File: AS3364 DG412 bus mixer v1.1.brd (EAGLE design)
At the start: 81.3 x 36.8 mm, 123 parts, among them IC1 PCA9539PW, IC10 DG412-J, IC11 DG412-J, IC2 TL074JT, IC3 TL072JT, IC4 TL074JT, IC5 TL072JT, IC6 TL072JT, IC8 DG412-J, IC9 DG412-J

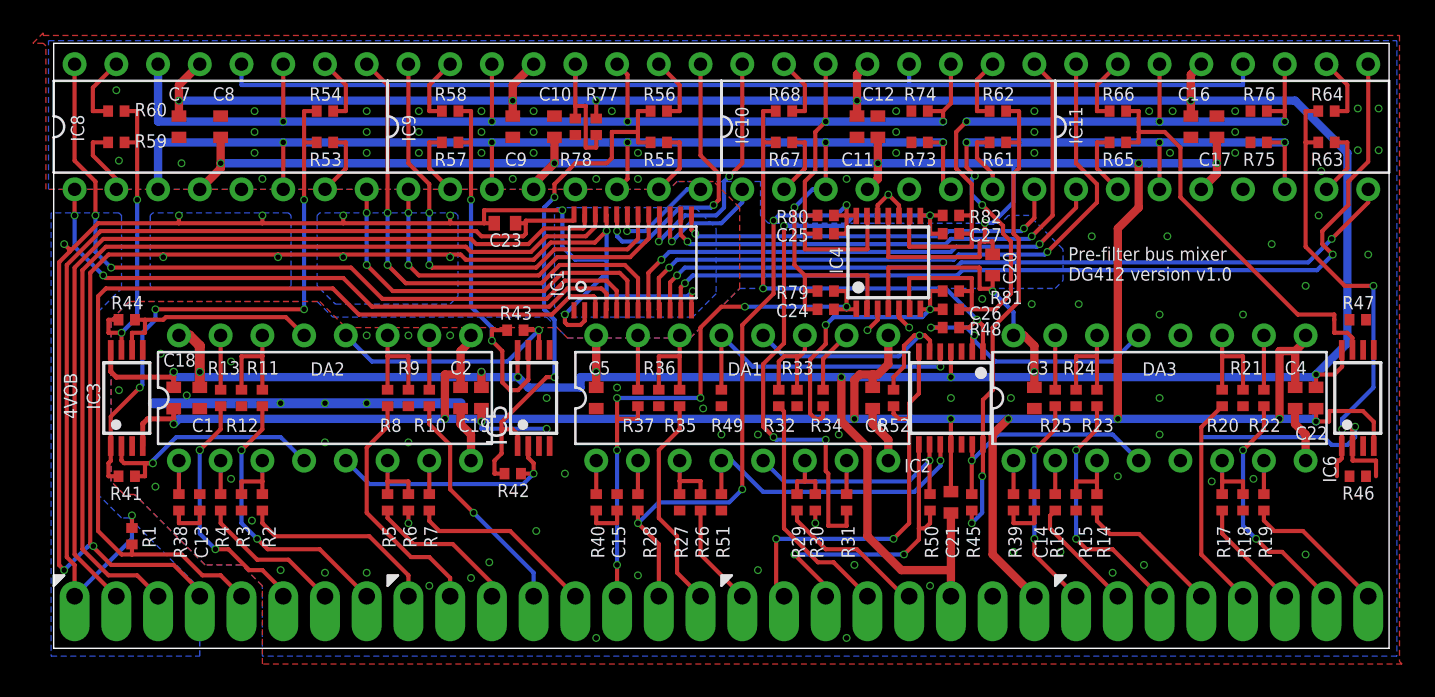
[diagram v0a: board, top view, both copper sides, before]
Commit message: Finished tracing v1.1 of DG412 bus mixer
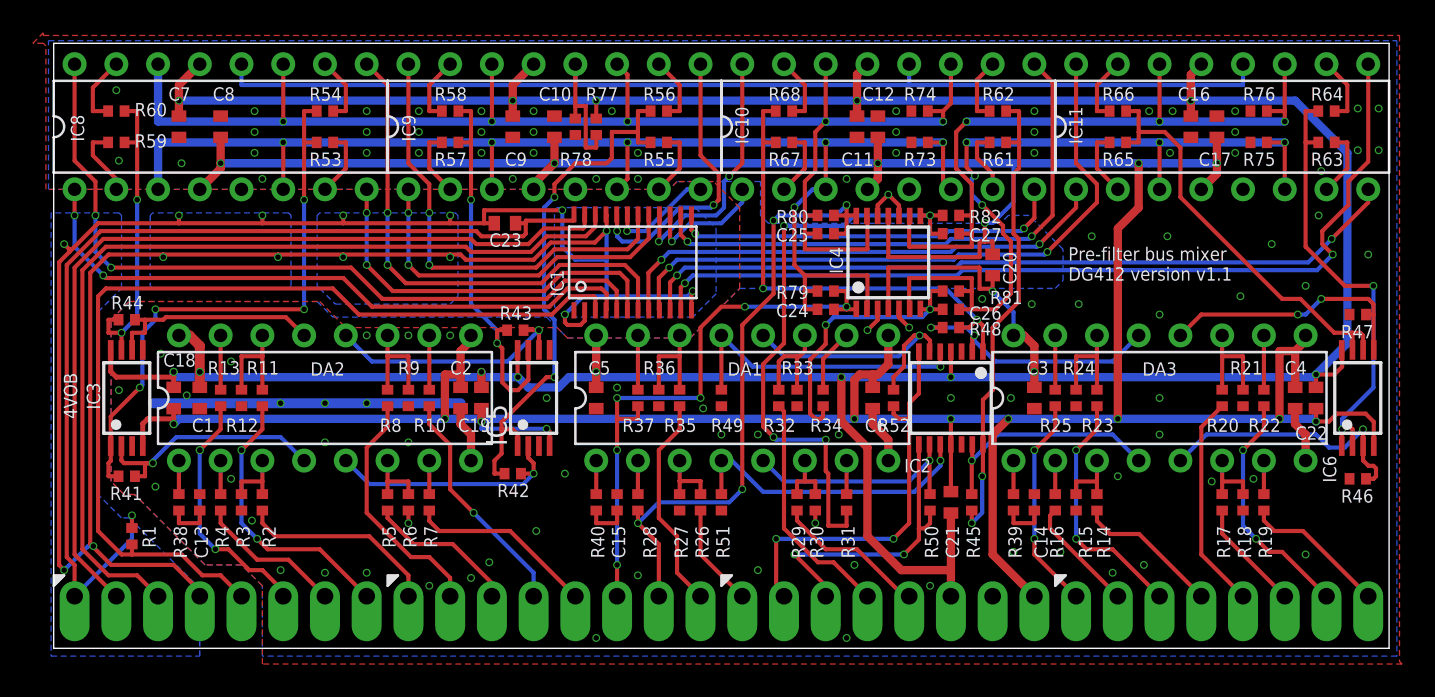
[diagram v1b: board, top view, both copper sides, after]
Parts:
- moved R47 0.32 mm to (79.4, 20.3), turned to 180 degrees
- moved R46 0.16 mm to (79.4, 10.3), turned to 180 degrees
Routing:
- net N$4: track 0.00 -> 16.6 mm, vias 0 -> 1
- net N$19: track 0.00 -> 16.1 mm, vias 0 -> 2
- net OUT8: track 42.3 -> 27.2 mm, vias 3 -> 2
- net OUT7: track 24.8 -> 25.9 mm
- net -12V: track 233.9 -> 234.5 mm
- net DGND: track 137.8 -> 137.2 mm
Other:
- board text added: "Pre-filter bus mixer DG412 version v1.1"
- board text removed: "Pre-filter bus mixer DG412 version v1.0"

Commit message: Tested bom ok
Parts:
- C13, C14, C15, C24, C25, C26, C27: device joakim:R0402 -> joakim:C0402-J
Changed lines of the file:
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@@
 <attribute name="VALUE" x="50.8" y="31.115" size="0.8128" layer="27" font="vector" rot="R90"/>
 </element>
-<element name="C13" library="joakim" package="R0402" package3d_urn="urn:adsk.eagle:package:23547/3" value="5nF" x="8.89" y="8.89" smashed="yes" rot="R270">
+<element name="C13" library="joakim" package="C0402-J" value="5nF" x="8.89" y="8.89" smashed="yes" rot="R270">
 <attribute name="NAME" x="8.5725" y="7.46125" size="0.8128" layer="25" font="vector" rot="R270"/>
 <attribute name="VALUE" x="6.985" y="9.525" size="0.8128" layer="27" font="vector" rot="R270"/>
 </element>
-<element name="C14" library="joakim" package="R0402" package3d_urn="urn:adsk.eagle:package:23547/3" value="5nF" x="59.69" y="8.89" smashed="yes" rot="R270">
+<element name="C14" library="joakim" package="C0402-J" value="5nF" x="59.69" y="8.89" smashed="yes" rot="R270">
 <attribute name="NAME" x="59.69" y="7.46125" size="0.8128" layer="25" font="vector" rot="R270"/>
 <attribute name="VALUE" x="57.785" y="9.525" size="0.8128" layer="27" font="vector" rot="R270"/>
 </element>
-<element name="C15" library="joakim" package="R0402" package3d_urn="urn:adsk.eagle:package:23547/3" value="5nF" x="34.29" y="8.89" smashed="yes" rot="R270">
+<element name="C15" library="joakim" package="C0402-J" value="5nF" x="34.29" y="8.89" smashed="yes" rot="R270">
 <attribute name="NAME" x="33.9725" y="7.46125" size="0.8128" layer="25" font="vector" rot="R270"/>
 <attribute name="VALUE" x="32.385" y="9.525" size="0.8128" layer="27" font="vector" rot="R270"/>
@@
 <attribute name="VALUE" x="40.64" y="-1.016" size="1.27" layer="27" ratio="10"/>
 </element>
-<element name="C24" library="joakim" package="R0402" package3d_urn="urn:adsk.eagle:package:23547/3" value="33pF" x="46.99" y="21.74875" smashed="yes">
+<element name="C24" library="joakim" package="C0402-J" value="33pF" x="46.99" y="21.74875" smashed="yes">
 <attribute name="NAME" x="43.97375" y="20.16125" size="0.8128" layer="25" font="vector"/>
 <attribute name="VALUE" x="46.355" y="19.84375" size="1.27" layer="27"/>
 </element>
-<element name="C25" library="joakim" package="R0402" package3d_urn="urn:adsk.eagle:package:23547/3" value="33pF" x="46.99" y="25.24125" smashed="yes">
+<element name="C25" library="joakim" package="C0402-J" value="33pF" x="46.99" y="25.24125" smashed="yes">
 <attribute name="NAME" x="43.97375" y="24.765" size="0.8128" layer="25" font="vector"/>
 <attribute name="VALUE" x="46.355" y="23.33625" size="1.27" layer="27"/>
 </element>
-<element name="C26" library="joakim" package="R0402" package3d_urn="urn:adsk.eagle:package:23547/3" value="33pF" x="54.61" y="21.74875" smashed="yes" rot="R180">
+<element name="C26" library="joakim" package="C0402-J" value="33pF" x="54.61" y="21.74875" smashed="yes" rot="R180">
 <attribute name="NAME" x="55.72125" y="20.0025" size="0.8128" layer="25" font="vector"/>
 <attribute name="VALUE" x="55.245" y="23.65375" size="1.27" layer="27" rot="R180"/>
 </element>
-<element name="C27" library="joakim" package="R0402" package3d_urn="urn:adsk.eagle:package:23547/3" value="33pF" x="54.61" y="25.24125" smashed="yes" rot="R180">
+<element name="C27" library="joakim" package="C0402-J" value="33pF" x="54.61" y="25.24125" smashed="yes" rot="R180">
 <attribute name="NAME" x="55.72125" y="24.765" size="0.8128" layer="25" font="vector"/>
 <attribute name="VALUE" x="55.245" y="27.14625" size="1.27" layer="27" rot="R180"/>

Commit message: Changed logic voltage resistor divider
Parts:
- R77: value 105k -> 47k
- R78: value 75k -> 33k
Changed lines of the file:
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@@
 <attribute name="VALUE" x="74.295" y="8.255" size="0.8128" layer="27" font="vector" rot="R90"/>
 </element>
-<element name="R78" library="rcl" library_urn="urn:adsk.eagle:library:334" package="R0402" package3d_urn="urn:adsk.eagle:package:23547/3" value="75k" x="31.75" y="31.75" smashed="yes" rot="R270">
+<element name="R78" library="rcl" library_urn="urn:adsk.eagle:library:334" package="R0402" package3d_urn="urn:adsk.eagle:package:23547/3" value="33k" x="31.75" y="31.75" smashed="yes" rot="R270">
 <attribute name="NAME" x="30.7975" y="29.36875" size="0.8128" layer="25" font="vector"/>
 <attribute name="POPULARITY" value="0" x="-30.48" y="-30.48" size="1.778" layer="27" rot="R270" display="off"/>
@@
 <attribute name="VALUE" x="72.7075" y="30.7975" size="0.8128" layer="27" font="vector"/>
 </element>
-<element name="R77" library="rcl" library_urn="urn:adsk.eagle:library:334" package="R0402" package3d_urn="urn:adsk.eagle:package:23547/3" value="105k" x="33.02" y="31.75" smashed="yes" rot="R270">
+<element name="R77" library="rcl" library_urn="urn:adsk.eagle:library:334" package="R0402" package3d_urn="urn:adsk.eagle:package:23547/3" value="47k" x="33.02" y="31.75" smashed="yes" rot="R270">
 <attribute name="NAME" x="32.385" y="33.3375" size="0.8128" layer="25" font="vector"/>
 <attribute name="POPULARITY" value="0" x="-34.29" y="15.24" size="1.778" layer="27" rot="R270" display="off"/>
